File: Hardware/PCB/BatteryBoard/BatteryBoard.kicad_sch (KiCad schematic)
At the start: 77 parts, among them J1 USB_C_Receptacle_USB2.0, J2 Thermistor, J3 Conn_01x07, J4 Conn_01x07, J5 Conn_01x07, J6 Conn_01x07, J7 Power, Q1 FDS4935A, Q2 FDS4935A, SW1 SW_SPDT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

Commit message: バッテリモジュール完成
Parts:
- removed J7: Power, Connector_AMASS:AMASS_XT30UPB-F_1x02_P5.0mm_Vertical, symbol Connector_Generic:Conn_01x02
- added D3: ESDA13P70-1U1M, Diode_SMD_extlib:ESDA13P70-1U1M, symbol Device:D_Zener_Small
- added J7: Power, Connector_PinHeader_2.54mm:PinHeader_1x04_P2.54mm_Vertical, symbol Connector_Generic:Conn_01x04
- C23: footprint Capacitor_SMD:C_1206_3216Metric -> Capacitor_SMD:C_0805_2012Metric
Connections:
- net +3.3V: now also J7.4 (Pin_4)
- net +5V: now also J7.1 (Pin_1)
- net GND: now also D3.2 (A), J7.2 (Pin_2), J7.3 (Pin_3)
- net VDD: now also D3.1 (K)
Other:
- moved on the sheet: H1, H2, H3, H4

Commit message: バッテリモジュールの部品表を生成
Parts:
- C1, C10, C7: value 10u(3225) -> 10μF100V X7S 3225
- C16, C17: value 10u(3225) -> 47μF16V X6S 3225
- C18, C19: value 0.1u -> 1u
- C22: value 10u(3216) -> 100μF10V X5R 3216
- C23: value 10u(3216) -> 10μF35V X5R 2012
- C24: value 22u(3216) -> 100μF10V X5R 3216
- C25: value 22u(3216) -> 220μF4V X6S 3216
- C30, C31: value 4.7u -> 4.7μF50V X7S 2012
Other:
- note added: "34uF @5V"
- note added: "88uF @3.3V"
- note added: "8uF @3.3V"
- moved on the sheet: C30, C31

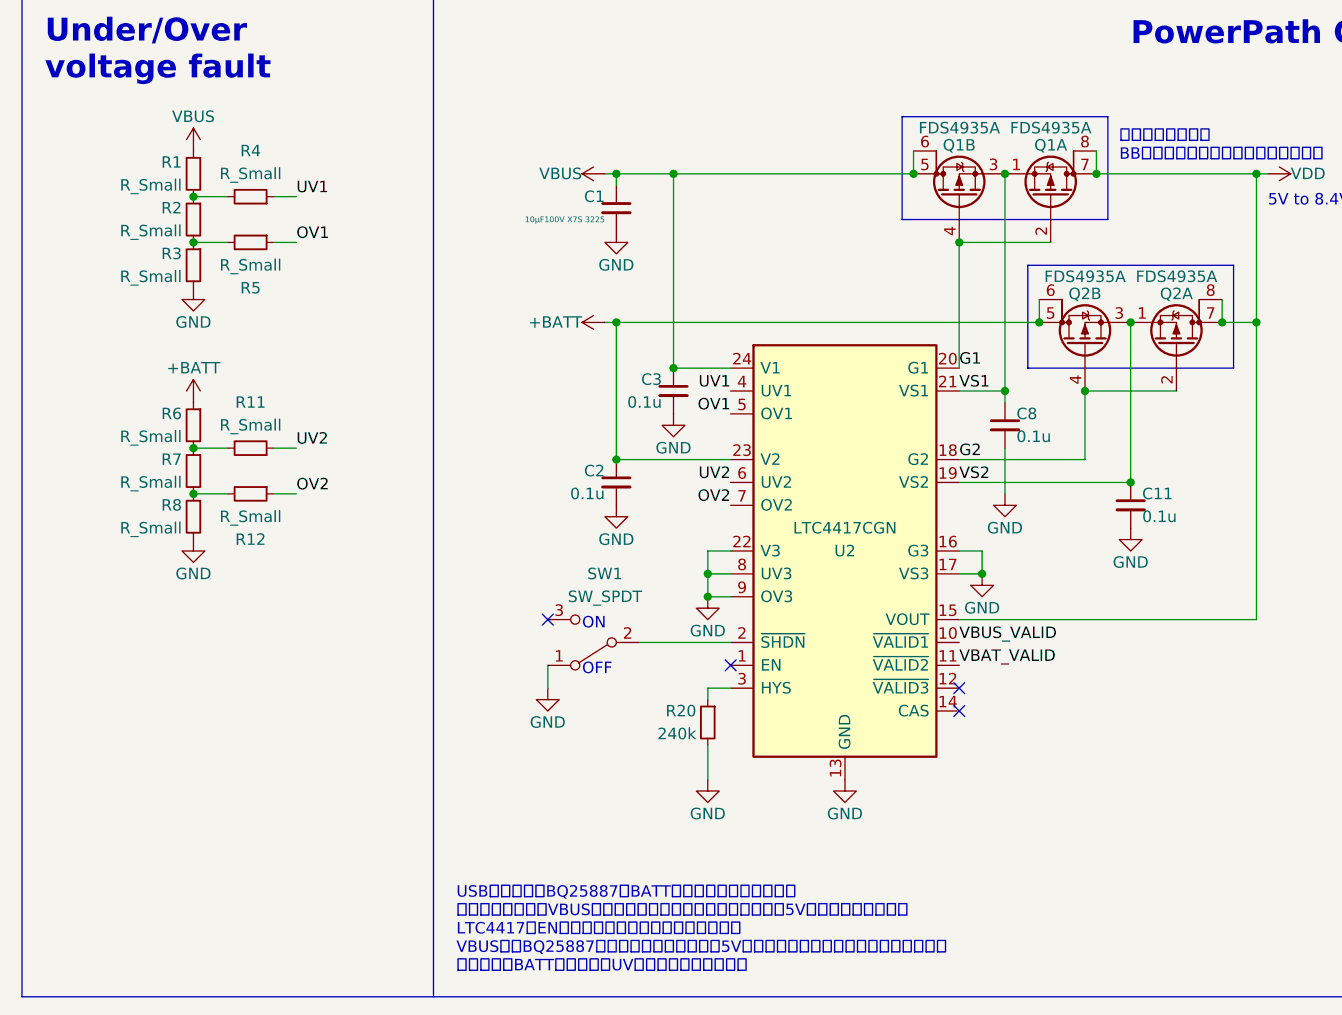
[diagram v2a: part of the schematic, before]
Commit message: ヒューズを追加、バッテリクリップの下のベタをBATTネットに
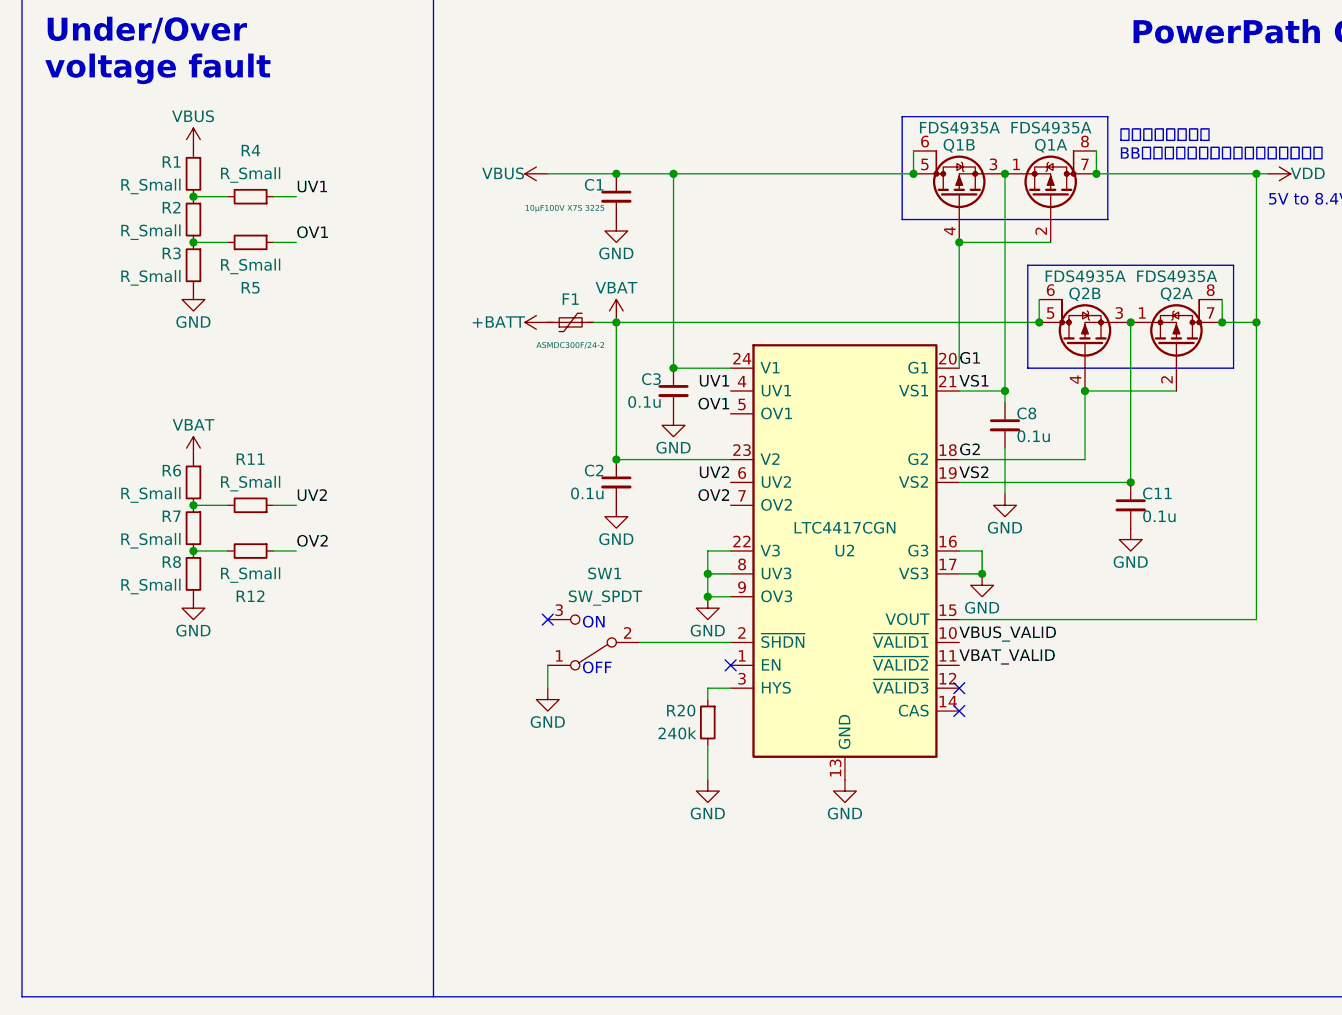
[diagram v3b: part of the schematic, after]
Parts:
- added F1: ASMDC300F/24-2, ASMDC300F_24-2:ASMDC300F_24-2, symbol Device:Polyfuse_Small
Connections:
- net +BATT: now also F1.1; no longer C2.1, Q2.5 (D), Q2.6 (G), R6.1, U2.23 (V2)
- new net VBAT: C2.1, F1.2, Q2.5 (D), Q2.6 (G), R6.1, U2.23 (V2)
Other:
- note removed: "USBが未接続でBQ25887がBATTから給電されている時に サーミスタ電源がVBUSでは使えないため、サーミスタ電源は5Vである必要がある。 LTC4417のENにスイッチを付けてオフにすると、 VBUSからBQ25887に給電、充電されるけど5Vサーミスタが使えないことになるので、 スイッチはBATT側につけてUVフォルトを作成する。"
- moved on the sheet: C1, R11, R12, R6, R7, R8

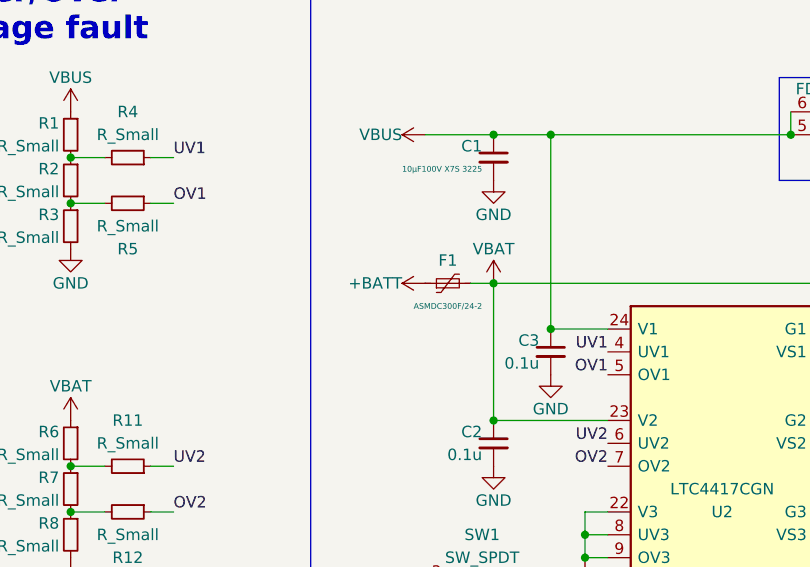
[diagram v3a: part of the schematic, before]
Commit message: 保護回路付きの18500が入るように変更
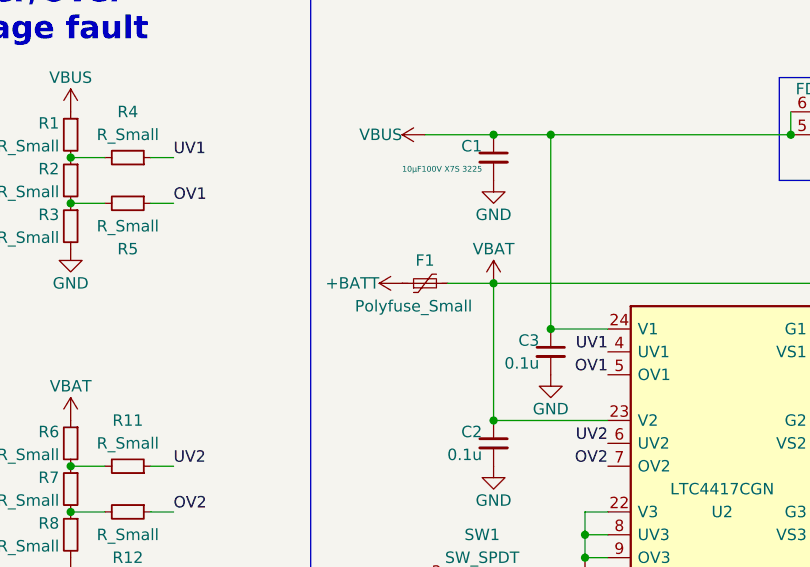
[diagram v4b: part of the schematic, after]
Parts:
- BT1, BT2: footprint Battery_extlib:BatteryClip_Keystone_18500 -> Battery_extlib:BatteryClip_Keystone_18500_Protected
- F1: value ASMDC300F/24-2 -> Polyfuse_Small
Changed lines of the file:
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@@
     (stroke (width 0) (type default) (color 0 0 0 0))
   )
-  (wire (pts (xy 77.47 120.65) (xy 80.01 120.65))
-    (stroke (width 0) (type default) (color 0 0 0 0))
-  )
   (wire (pts (xy 118.11 40.64) (xy 119.38 40.64))
     (stroke (width 0) (type default) (color 0 0 0 0))
@@
     (stroke (width 0) (type default) (color 0 0 0 0))
   )
+  (wire (pts (xy 74.93 120.65) (xy 80.01 120.65))
+    (stroke (width 0) (type default) (color 0 0 0 0))
+  )
   (wire (pts (xy 113.03 58.42) (xy 113.03 66.04))
     (stroke (width 0) (type default) (color 0 0 0 0))
@@
       (effects (font (size 1.27 1.27)) (justify left))
     )
-    (property "Footprint" "Battery_extlib:BatteryClip_Keystone_18500" (id 2) (at 125.73 54.356 90)
+    (property "Footprint" "Battery_extlib:BatteryClip_Keystone_18500_Protected" (id 2) (at 125.73 54.356 90)
       (effects (font (size 1.27 1.27)) hide)
     )
@@
     (pin "1")
   )
-  (symbol (lib_id "power:+BATT") (at 72.39 120.65 90) (unit 1)
+  (symbol (lib_id "power:+BATT") (at 69.85 120.65 90) (unit 1)
     (in_bom yes) (on_board yes)
-    (property "Reference" "#PWR013" (id 0) (at 76.2 120.65 0)
+    (property "Reference" "#PWR013" (id 0) (at 73.66 120.65 0)
       (effects (font (size 1.27 1.27)) hide)
     )
-    (property "Value" "+BATT" (id 1) (at 69.85 120.65 90)
+    (property "Value" "+BATT" (id 1) (at 67.31 120.65 90)
       (effects (font (size 1.27 1.27)) (justify left))
     )
-    (property "Footprint" "" (id 2) (at 72.39 120.65 0)
+    (property "Footprint" "" (id 2) (at 69.85 120.65 0)
       (effects (font (size 1.27 1.27)) hide)
     )
-    (property "Datasheet" "" (id 3) (at 72.39 120.65 0)
+    (property "Datasheet" "" (id 3) (at 69.85 120.65 0)
       (effects (font (size 1.27 1.27)) hide)
     )
@@
     (pin "1")
   )
-  (symbol (lib_id "power:VBUS") (at 100.33 20.32 0) (unit 1)
-    (in_bom yes) (on_board yes)
-    (property "Reference" "#PWR021" (id 0) (at 100.33 24.13 0)
+  (symbol (lib_id "power_extlib:VBAT") (at 80.01 120.65 0) (unit 1)
+    (in_bom no) (on_board no)
+    (property "Reference" "#PWR071" (id 0) (at 83.82 119.38 0)
       (effects (font (size 1.27 1.27)) hide)
     )
-    (property "Value" "VBUS" (id 1) (at 100.33 16.51 0))
-    (property "Footprint" "" (id 2) (at 100.33 20.32 0)
+    (property "Value" "VBAT" (id 1) (at 80.01 116.84 0))
+    (property "Footprint" "" (id 2) (at 81.788 120.65 0)
       (effects (font (size 1.27 1.27)) hide)
     )
-    (property "Datasheet" "" (id 3) (at 100.33 20.32 0)
+    (property "Datasheet" "" (id 3) (at 81.788 120.65 0)
       (effects (font (size 1.27 1.27)) hide)
     )
     (pin "1")
   )
-  (symbol (lib_id "power_extlib:VBAT") (at 33.02 135.89 0) (unit 1)
-    (in_bom no) (on_board no)
-    (property "Reference" "#PWR05" (id 0) (at 36.83 134.62 0)
+  (symbol (lib_id "power:VBUS") (at 100.33 20.32 0) (unit 1)
+    (in_bom yes) (on_board yes)
+    (property "Reference" "#PWR021" (id 0) (at 100.33 24.13 0)
       (effects (font (size 1.27 1.27)) hide)
     )
-    (property "Value" "VBAT" (id 1) (at 33.02 132.08 0))
-    (property "Footprint" "" (id 2) (at 34.798 135.89 0)
+    (property "Value" "VBUS" (id 1) (at 100.33 16.51 0))
+    (property "Footprint" "" (id 2) (at 100.33 20.32 0)
       (effects (font (size 1.27 1.27)) hide)
     )
-    (property "Datasheet" "" (id 3) (at 34.798 135.89 0)
+    (property "Datasheet" "" (id 3) (at 100.33 20.32 0)
       (effects (font (size 1.27 1.27)) hide)
     )
@@
     (pin "2")
   )
-  (symbol (lib_id "Device:Polyfuse_Small") (at 74.93 120.65 90) (unit 1)
-    (in_bom yes) (on_board yes)
-    (property "Reference" "F1" (id 0) (at 74.93 118.11 90))
-    (property "Value" "ASMDC300F/24-2" (id 1) (at 74.93 123.19 90)
-      (effects (font (size 0.635 0.635)))
-    )
-    (property "Footprint" "ASMDC300F_24-2:ASMDC300F_24-2" (id 2) (at 80.01 119.38 0)
-      (effects (font (size 1.27 1.27)) (justify left) hide)
-    )
-    (property "Datasheet" "~" (id 3) (at 74.93 120.65 0)
-      (effects (font (size 1.27 1.27)) hide)
-    )
-    (pin "1")
-    (pin "2")
-  )
   (symbol (lib_id "power:GND") (at 279.4 31.75 0) (unit 1)
     (in_bom yes) (on_board yes)
@@
       (effects (font (size 1.27 1.27)) (justify left))
     )
-    (property "Footprint" "Battery_extlib:BatteryClip_Keystone_18500" (id 2) (at 125.73 67.056 90)
+    (property "Footprint" "Battery_extlib:BatteryClip_Keystone_18500_Protected" (id 2) (at 125.73 67.056 90)
       (effects (font (size 1.27 1.27)) hide)
     )
@@
     (pin "2")
   )
-  (symbol (lib_id "power_extlib:VBAT") (at 80.01 120.65 0) (unit 1)
-    (in_bom no) (on_board no)
-    (property "Reference" "#PWR071" (id 0) (at 83.82 119.38 0)
-      (effects (font (size 1.27 1.27)) hide)
-    )
-    (property "Value" "VBAT" (id 1) (at 80.01 116.84 0))
-    (property "Footprint" "" (id 2) (at 81.788 120.65 0)
-      (effects (font (size 1.27 1.27)) hide)
-    )
-    (property "Datasheet" "" (id 3) (at 81.788 120.65 0)
-      (effects (font (size 1.27 1.27)) hide)
-    )
-    (pin "1")
-  )
   (symbol (lib_id "Device:C_Small") (at 123.19 132.08 0) (unit 1)
     (in_bom yes) (on_board yes)
@@
     (pin "2")
   )
+  (symbol (lib_id "Device:Polyfuse_Small") (at 72.39 120.65 90) (unit 1)
+    (in_bom yes) (on_board yes)
+    (property "Reference" "F1" (id 0) (at 72.39 118.11 90))
+    (property "Value" "Polyfuse_Small" (id 1) (at 71.12 123.19 90))
+    (property "Footprint" "ASMDC300F_24-2:ASMDC300F_24-2" (id 2) (at 77.47 119.38 0)
+      (effects (font (size 1.27 1.27)) (justify left) hide)
+    )
+    (property "Datasheet" "~" (id 3) (at 72.39 120.65 0)
+      (effects (font (size 1.27 1.27)) hide)
+    )
+    (pin "1")
+    (pin "2")
+  )
   (symbol (lib_id "Device:R_Small") (at 33.02 109.22 0) (mirror y) (unit 1)
     (in_bom yes) (on_board yes)
@@
     (pin "2")
   )
+  (symbol (lib_id "power_extlib:VBAT") (at 33.02 135.89 0) (unit 1)
+    (in_bom no) (on_board no)
+    (property "Reference" "#PWR05" (id 0) (at 36.83 134.62 0)
+      (effects (font (size 1.27 1.27)) hide)
+    )
+    (property "Value" "VBAT" (id 1) (at 33.02 132.08 0))
+    (property "Footprint" "" (id 2) (at 34.798 135.89 0)
+      (effects (font (size 1.27 1.27)) hide)
+    )
+    (property "Datasheet" "" (id 3) (at 34.798 135.89 0)
+      (effects (font (size 1.27 1.27)) hide)
+    )
+    (pin "1")
+  )
   (symbol (lib_id "power:GND") (at 119.38 53.34 0) (unit 1)
     (in_bom yes) (on_board yes)
@@
       (reference "#PWR04") (unit 1) (value "GND") (footprint "")
     )
-    (path "/6b92f2e4-ca59-4ba7-a74f-d45a9fde7614"
+    (path "/f933bb44-6669-4844-af90-9a0922e71ea1"
       (reference "#PWR05") (unit 1) (value "VBAT") (footprint "")
     )
@@
       (reference "#PWR070") (unit 1) (value "GND") (footprint "")
     )
-    (path "/eeec722a-3914-4d7c-9ca4-82d6e1ba7c4b"
+    (path "/66f1aab3-8633-4788-bbfc-327112d029d6"
       (reference "#PWR071") (unit 1) (value "VBAT") (footprint "")
     )
@@
     )
     (path "/3b6cec1c-3144-4154-90a6-72bac8893014"
-      (reference "BT1") (unit 1) (value "BATT") (footprint "Battery_extlib:BatteryClip_Keystone_18500")
+      (reference "BT1") (unit 1) (value "BATT") (footprint "Battery_extlib:BatteryClip_Keystone_18500_Protected")
     )
     (path "/e5d9a4e9-7c6a-41e6-89b3-cba57ed78c7a"
-      (reference "BT2") (unit 1) (value "BATT") (footprint "Battery_extlib:BatteryClip_Keystone_18500")
+      (reference "BT2") (unit 1) (value "BATT") (footprint "Battery_extlib:BatteryClip_Keystone_18500_Protected")
     )
     (path "/d7e0076c-dbf4-4d54-bf17-7a915b7a4662"
@@
       (reference "D3") (unit 1) (value "ESDA13P70-1U1M") (footprint "Diode_SMD_extlib:ESDA13P70-1U1M")
     )
-    (path "/bb91455c-6e04-4ca8-9749-02a21da0b682"
-      (reference "F1") (unit 1) (value "ASMDC300F/24-2") (footprint "ASMDC300F_24-2:ASMDC300F_24-2")
+    (path "/f1f15a2e-04e4-40e7-b763-d2503573dbf7"
+      (reference "F1") (unit 1) (value "Polyfuse_Small") (footprint "ASMDC300F_24-2:ASMDC300F_24-2")
     )
     (path "/86dcfadf-4bc2-429b-86ed-fc2db247e055"
